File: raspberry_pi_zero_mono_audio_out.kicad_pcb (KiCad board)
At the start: 2 copper layers, 25.7 x 16.5 mm, 6 parts, among them J1 AudioJack2_SwitchT, J2 Conn_01x02

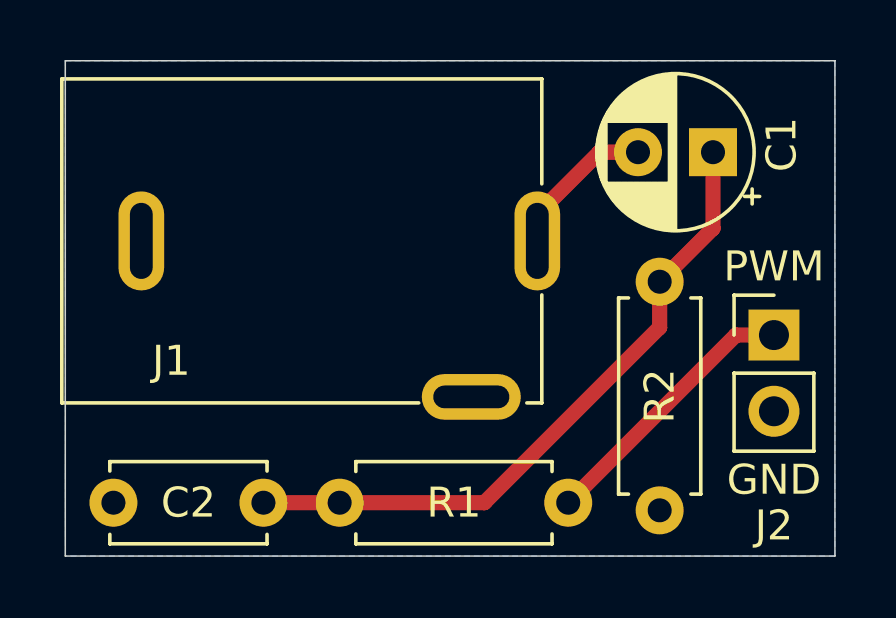
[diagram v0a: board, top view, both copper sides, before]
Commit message: Update silkscreen with github URL
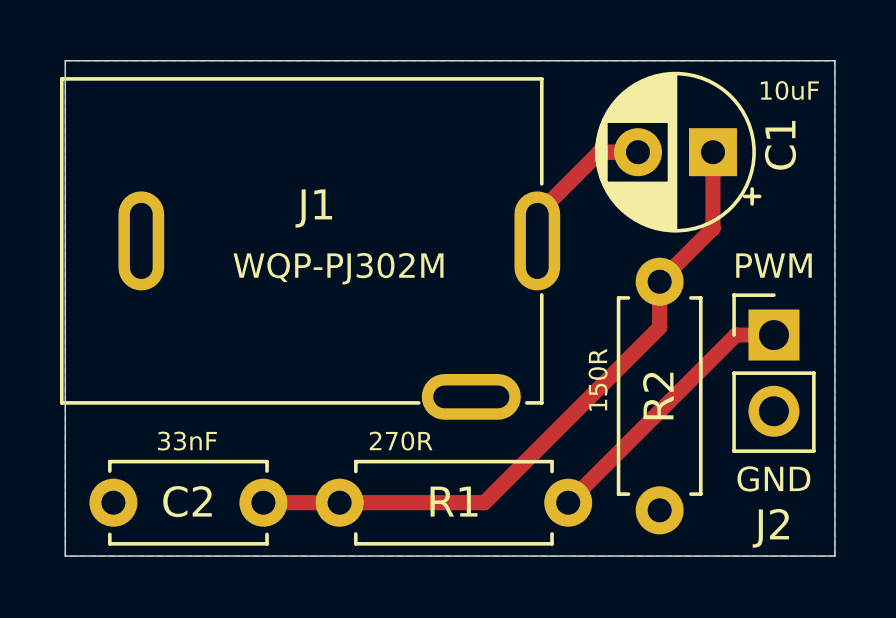
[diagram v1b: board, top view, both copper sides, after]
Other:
- board text added: "10uF"
- board text added: "150R"
- board text added: "270R"
- board text added: "33nF"
- board text added: "Raspberry Pi Zero Mono Audio Output"
- board text added: "WQP-PJ302M"
- board text added: "github.com/joem"
- board text removed: "RPi Zero Mono Audio v1 JWM"
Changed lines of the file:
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@@
   (general
     (thickness 1.6)
-    (drawings 7)
+    (drawings 13)
     (tracks 12)
     (zones 0)
@@
     (descr "TRS 3.5mm, horizontal, PCB mount, WQP-PJ302M, (http://www.qingpu-electronics.com/en/products/WQP-PJ302M-57.html)")
     (tags "WQP-PJ302M TRS 3.5mm mono horizontal qingpu jack")
-    (fp_text reference J1 (at -4.35 4) (layer F.SilkS)
+    (fp_text reference J1 (at 0.498775 -1.179) (layer F.SilkS)
       (effects (font (size 1 1) (thickness 0.15)))
     )
@@
     )
   )
+  (gr_text github.com/joem (at 149.86 91.186) (layer B.SilkS)
+    (effects (font (size 1 1) (thickness 0.15)) (justify mirror))
+  )
+  (gr_text 150R (at 159.258 92.964 90) (layer F.SilkS)
+    (effects (font (size 0.6096 0.6096) (thickness 0.0508)))
+  )
+  (gr_text 10uF (at 165.608 83.312) (layer F.SilkS)
+    (effects (font (size 0.6096 0.6096) (thickness 0.0508)))
+  )
+  (gr_text 270R (at 152.654 94.996) (layer F.SilkS)
+    (effects (font (size 0.6096 0.6096) (thickness 0.0508)))
+  )
+  (gr_text 33nF (at 145.542 94.996) (layer F.SilkS)
+    (effects (font (size 0.6096 0.6096) (thickness 0.0508)))
+  )
+  (gr_text WQP-PJ302M (at 150.622 89.154) (layer F.SilkS)
+    (effects (font (size 0.8128 0.8128) (thickness 0.127)))
+  )
   (gr_text PWM (at 165.1 89.154) (layer F.SilkS)
-    (effects (font (size 1 1) (thickness 0.15)))
+    (effects (font (size 0.8128 0.8128) (thickness 0.127)))
   )
   (gr_text GND (at 165.1 96.266) (layer F.SilkS)
-    (effects (font (size 1 1) (thickness 0.15)))
-  )
-  (gr_text "RPi Zero\nMono Audio\nv1\nJWM" (at 150.622 88.138) (layer B.SilkS)
+    (effects (font (size 0.8128 0.8128) (thickness 0.127)))
+  )
+  (gr_text "Raspberry Pi Zero\nMono Audio Output" (at 150.876 84.328) (layer B.SilkS)
     (effects (font (size 1 1) (thickness 0.15)) (justify mirror))
   )

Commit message: Update project to kicad 6+
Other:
- net class Default removed
